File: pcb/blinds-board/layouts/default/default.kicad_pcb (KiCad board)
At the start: 2 copper layers, 87 parts

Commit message: feat(blinds-pcb): 6-layer placement + A* routing, board fully routed
tools/router.py is an A* grid router over the copper layers; place_and_render
holds the anchors, the passive banks and the fanout. 87 footprints, 62 routed
nets, 9241 segments, 238 vias, nothing left unrouted.

What it took, in the order the board taught it:
  * 6 layers (F/In1 GND/In2/In3/In4 GND/B). 24 nets escape a 4mm 29-pin QFN;
    two routing layers cannot do it and three got within a few nets.
  * Fanout stubs per fine-pitch pad, staggered over four depths, each ending
    in a via. Without the via the escapes stay 0.4mm apart forever and none of
    them can ever change layer — which is what stranded the last net.
  * L-shaped corner pads rasterised, not bounding-boxed: the box fills in the
    notch the neighbouring pin escapes through.
  * Clearance is width-aware at query time, so a 0.6mm rail cannot be laid at
    a 0.15mm track's clearance. That was a real short, found by DRC.
  * Local decoupling for PMID, BATP and REGN — a sense pin on the far flank of
    a QFN wants copper 3mm away, not 8.
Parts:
- J1: footprint USB_C_16P:USB-C_SMD-TYPE-C-31-M-12_1 -> XH_3AW:CONN-TH_3P-P2.50_XH-3A
- J4: footprint XH_3AW:CONN-TH_3P-P2.50_XH-3A -> XH_2AW:CONN-TH_2P-P2.50_XH-2AW
- J5: footprint XH_2AW:CONN-TH_2P-P2.50_XH-2AW -> USB_C_16P:USB-C_SMD-TYPE-C-31-M-12_1
- U2: footprint ESP32_C3_MINI_1:WIFIM-SMD_ESP32-C3-MINI-1 -> TLV62569DBVR:SOT-23-5_L3.0-W1.7-P0.95-LS2.8-BR
- U3: footprint TLV62569DBVR:SOT-23-5_L3.0-W1.7-P0.95-LS2.8-BR -> BQ25798RQMR:QFN-29_L4.0-W4.0-P0.40-TL-BQ25792RQMR
- U4: footprint BQ25798RQMR:QFN-29_L4.0-W4.0-P0.40-TL-BQ25792RQMR -> DRV8871DDAR:SO-8_L4.9-W3.9-P1.27-LS6.0-BL-EP
- U5: footprint DRV8871DDAR:SO-8_L4.9-W3.9-P1.27-LS6.0-BL-EP -> DRV5032FBDBZR:SOT-23_L2.9-W1.3-P1.90-LS2.4-BR
- U6: footprint DRV5032FBDBZR:SOT-23_L2.9-W1.3-P1.90-LS2.4-BR -> ESP32_C3_MINI_1:WIFIM-SMD_ESP32-C3-MINI-1
- moved U6 809.6 mm to (10.5, 12.0)
- moved C20 809.5 mm to (24.0, 75.5)
- moved J3 808.6 mm to (4.00, 64.8)
- moved J4 768.7 mm to (34.0, 64.8), turned to 180 degrees
- moved C22 763.3 mm to (7.00, 21.2)
- moved SW1 758.1 mm to (32.0, 14.3)
- moved C23 749.9 mm to (10.4, 21.2)
- moved SW2 748.0 mm to (32.0, 7.60)
- moved C21 747.9 mm to (2.40, 21.2)
- moved R20 719.7 mm to (20.6, 21.2)
- moved C18 713.1 mm to (17.2, 21.2)
- moved R9 706.5 mm to (13.8, 21.2)
- moved C11 685.7 mm to (16.5, 55.0)
- moved C13 683.3 mm to (29.0, 56.4)
- moved C12 663.2 mm to (29.0, 54.0)
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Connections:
- C20 pad 1: 1-3 -> 1-5
- C20 pad 2: 2 -> gnd_tab
- C28 pad 1: 1-5 -> 1-6
- J1 pad 1: 2 -> 1
- J1 pad 2: 2 -> batmid
- J2 pad 1: 1 -> 1-5
- J2 pad 2: batmid -> gnd_tab
- J2 pad 3: 2 -> hall_do_tab
- J4 pad 1: 1-3 -> mot_a
- J4 pad 2: 2 -> mot_b
- J5 pad 1: mot_a -> 2
- J5 pad 2: mot_b -> 2
- R16 pad 1: 1-6 -> 1-7
- R23 pad 1: 1-5 -> 1-6
- R27 pad 1: 1-5 -> 1-6
- U2 pad 1: 2 -> en_buck
- U2 pad 3: 1-3 -> sw_buck
- U2 pad 4: (no net) -> 1-2
- U2 pad 5: io2 -> fb_buck
- U3 pad 1: en_buck -> chg_stat
- U3 pad 2: 2 -> VBUS
- U3 pad 3: sw_buck -> VBUS
- U3 pad 4: 1-2 -> btst1
- U3 pad 5: fb_buck -> 1-6
- U4 pad 1: chg_stat -> 2
- U4 pad 2: VBUS -> 19
- U4 pad 3: VBUS -> 18
- U4 pad 4: btst1 -> ilim_mot
- U4 pad 5: 1-5 -> 1-1
- U4 pad 6: DP -> mot_a
- U4 pad 7: DM -> 2
- U4 pad 8: VBUS -> mot_b
- U4 pad 9: VBUS -> 2
- U5 pad 1: 2 -> 1-5
- U5 pad 2: 19 -> hall_do_tab
- U5 pad 3: 18 -> gnd_tab
- U6 pad 1: 1-3 -> 2
- U6 pad 2: hall_do -> 2
- U6 pad 3: 2 -> 1-3
- U7 pad 7: 1-6 -> 1-7
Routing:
- net 1-3: track 0.00 -> 110.0 mm, vias 0 -> 17
- net 18: track 0.00 -> 86.5 mm, vias 0 -> 3
- net 1-2: track 0.00 -> 83.3 mm, vias 0 -> 8
- net 2: track 0.00 -> 79.1 mm, vias 0 -> 54
- net 19: track 0.00 -> 75.6 mm, vias 0 -> 4
- net usb_dp: track 0.00 -> 70.6 mm, vias 0 -> 2
- net VBUS: track 0.00 -> 68.8 mm, vias 0 -> 12
- net 1: track 0.00 -> 59.0 mm, vias 0 -> 8
- net usb_dn: track 0.00 -> 58.4 mm, vias 0 -> 4
- net 2-2: track 0.00 -> 57.5 mm, vias 0 -> 3
- net hall_do: track 0.00 -> 57.2 mm, vias 0 -> 3
- net 1-1: track 0.00 -> 56.8 mm, vias 0 -> 9
- net en_bst: track 0.00 -> 41.4 mm, vias 0 -> 5
- net btn_up: track 0.00 -> 40.0 mm, vias 0 -> 2
- net sw_chg1: track 0.00 -> 39.6 mm, vias 0 -> 4
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- added copper zone on B.Cu, net gnd
- added copper zone on F.Cu, net gnd
- added copper zone on In1.Cu, net gnd
- added copper zone on In4.Cu, net gnd
- added copper zone on B.Cu, net gnd_tab
- added copper zone on F.Cu, net gnd_tab
- added copper zone on In1.Cu, net gnd_tab
- added copper zone on In4.Cu, net gnd_tab
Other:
- board outline added: 38 x 81 mm
- copper layers 2 -> 6
- rule pad_to_mask_clearance: 0 -> 0.05
- board text added: "0x63616c"
- board text added: "BAT 2S + M -"
- board text added: "BLINDS DRIVER rev B"
- board text added: "DOWN"
- board text added: "HALL"
- board text added: "HALL TAB - snap off"
- board text added: "MOTOR"
- board text added: "UP"
- board text added: "USB-C PD"

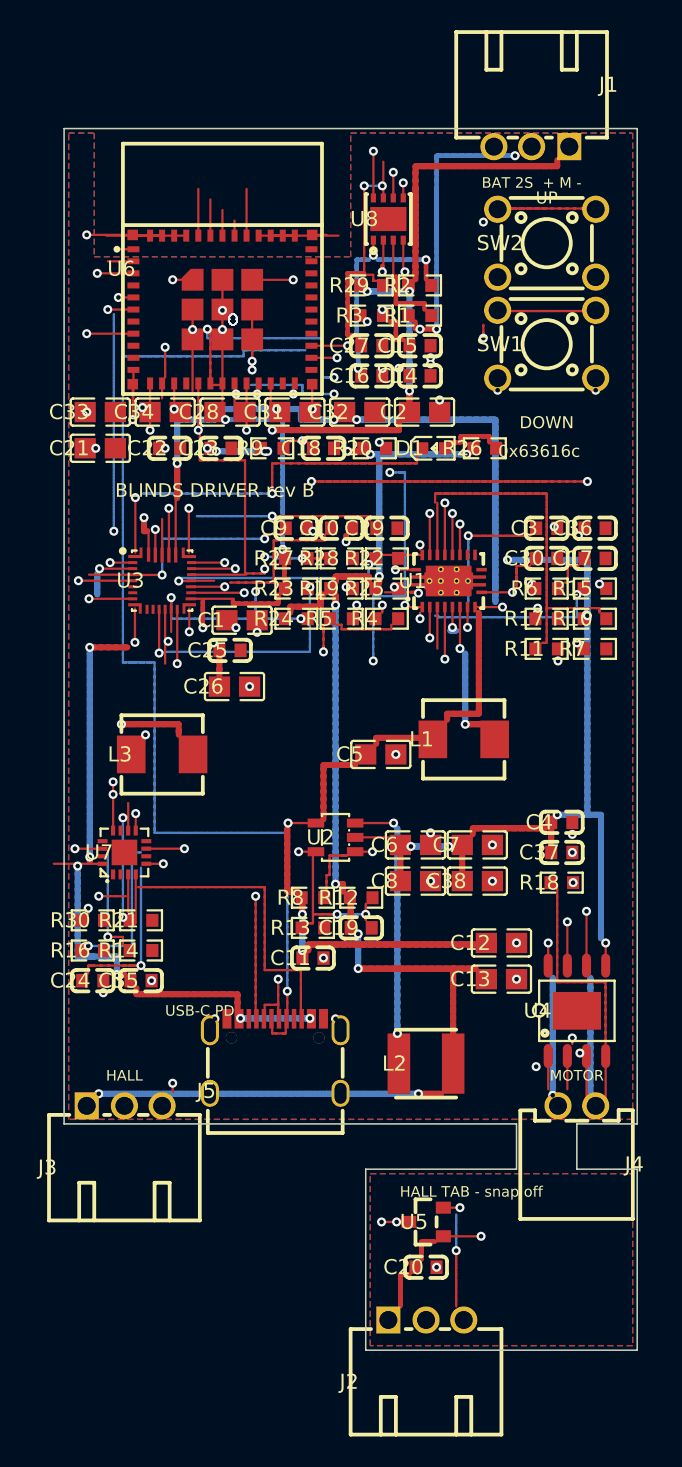
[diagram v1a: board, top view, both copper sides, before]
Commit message: feat(blinds-pcb): fab outputs, courtyards, silk trim, DRC harness
Adds the pieces the fab package needs and the checks that judge it:
  * courtyards on all 43 vendored footprints (add_courtyards.py) — KiCad ships
    missing_courtyard as an IGNORED check, so a board with none passes DRC
    while the overlap check silently never runs
  * silk trimmed back out of pads, once, per trim_lib_silk's warning
  * fix_vendor_pads.py: the TPS61088's eight netless 0.2mm thermal vias become
    PGND at 0.55/0.3, the USB-C's two mounting posts become non-plated
  * build_outputs.sh writes a net_settings block — DRC checks the NETCLASS
    clearance, and KiCad's built-in default of 0.2mm flagged every trace on a
    board designed to 0.13
  * gerbers (6 layers), drill, BOM, CPL and renders in fab/ and render/

DRC is NOT clean yet: 184 violations and 65 unconnected pads remain, mostly
marginal overlaps around through-hole pads and ground pads the pour does not
reach. Routing is 2 connections short. See issue #22 for the specifics.
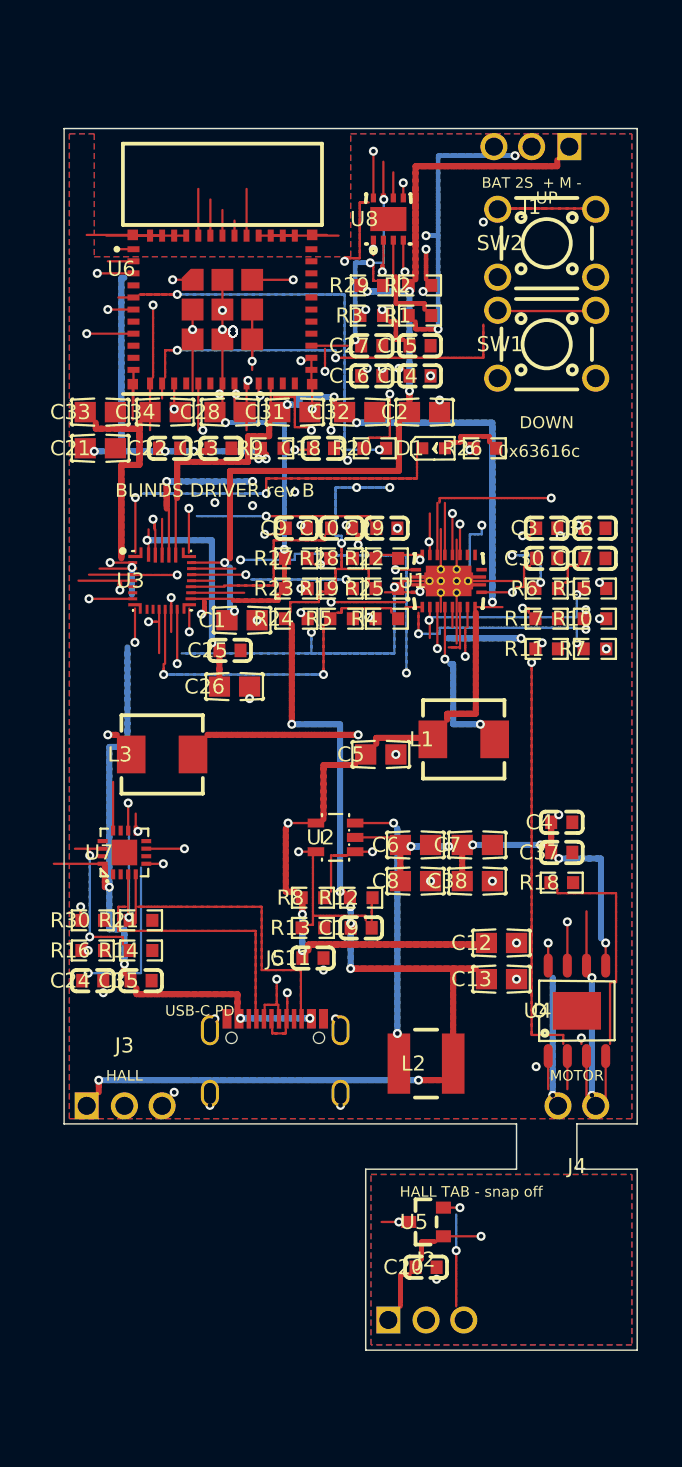
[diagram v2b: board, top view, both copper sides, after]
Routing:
- net 1-3: track 110.0 -> 129.3 mm, vias 17 -> 18
- net 2: track 79.1 -> 97.7 mm, vias 54 -> 45
- net 2-2: track 57.5 -> 42.9 mm, vias 3 -> 5
- net prog: track 15.8 -> 1.50 mm, vias 2 -> 0
- net 18: track 86.5 -> 73.1 mm, vias 3 -> 5
- net usb_dp: track 70.6 -> 57.4 mm, vias 2 -> 3
- net 1-6: track 33.1 -> 40.5 mm
- net batmid: track 22.8 -> 29.9 mm
- net sw_chg1: track 39.6 -> 32.8 mm
- net sda: track 36.6 -> 43.3 mm, vias 3 -> 4
- net 19: track 75.6 -> 69.4 mm, vias 4 -> 2
- net boot_bst: track 9.85 -> 15.5 mm
- net 1-1: track 56.8 -> 61.9 mm, vias 9 -> 11
- net chg_int: track 27.1 -> 22.8 mm
- net CC1: track 22.2 -> 18.9 mm, vias 2 -> 0
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- added copper zone on B.Cu, net 2
- added copper zone on F.Cu, net 2
- added copper zone on In1.Cu, net 2
- added copper zone on In4.Cu, net 2
- removed copper zone on B.Cu, net gnd
- removed copper zone on F.Cu, net gnd
- removed copper zone on In1.Cu, net gnd
- removed copper zone on In4.Cu, net gnd

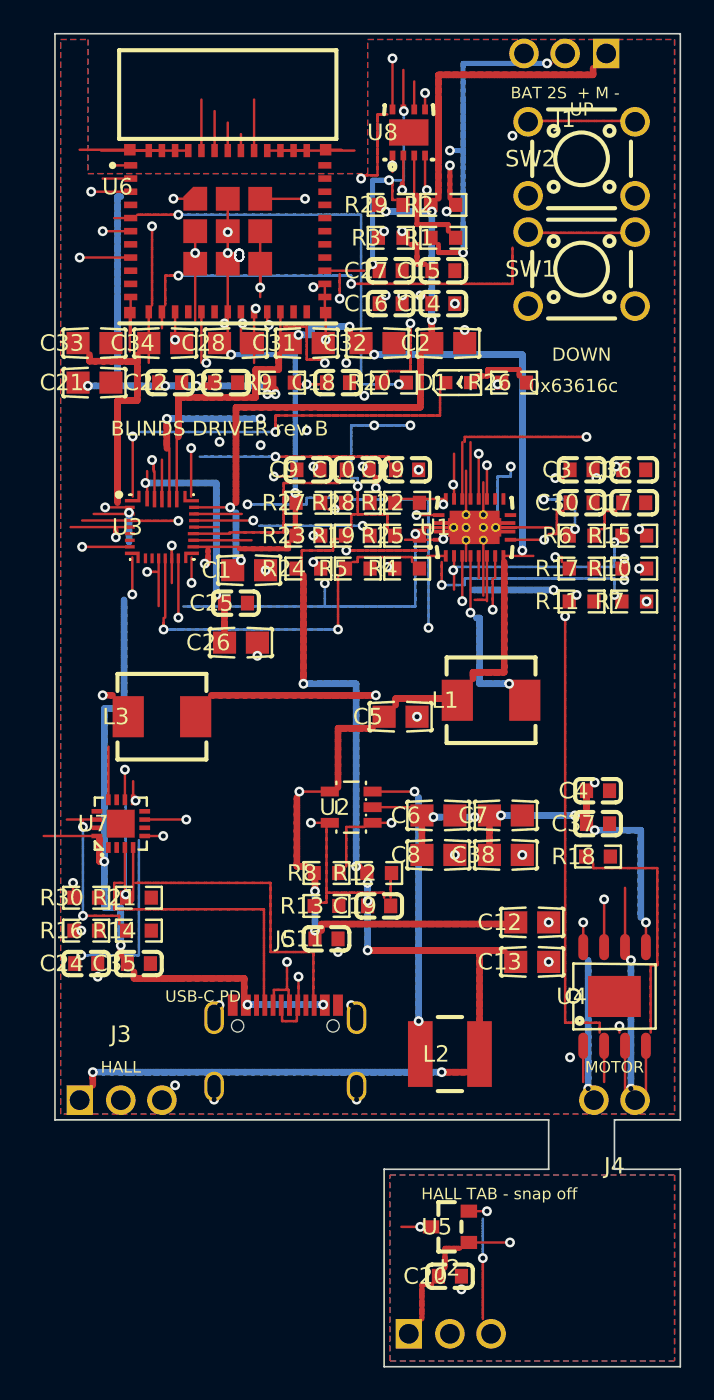
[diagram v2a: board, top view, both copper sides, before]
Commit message: fix(blinds-pcb): five router bugs that DRC was reporting as 350 violations
Down to 37 from 350. Each one was a modelling error, not a hundred separate
layout problems:

  * pad.layers was read with str(), which on a pyzig list gives its object
    repr — so EVERY pad fell back to F.Cu alone and the router ran tracks
    through every through-hole pad on the inner and bottom layers
  * trim_lib_silk leaves a zero-length layerless fp_line behind for each silk
    segment it clips away; a layerless line inherits the footprint's layer,
    which is F.Cu, so 28 of them were netless copper on the connectors
  * pad_shape was keyed by pad NAME, and the TPS61088 has nine pads called 21
    (the land plus eight thermal vias) — only the last one got a clearance halo
  * routes could start or end on halo cells, which carry the net id but are not
    copper, so some tracks were emitted floating
  * netless pads were blocked with clearance but no allowance for track width

Fab package (6-layer gerbers, drill, BOM, CPL) regenerated in fab/.
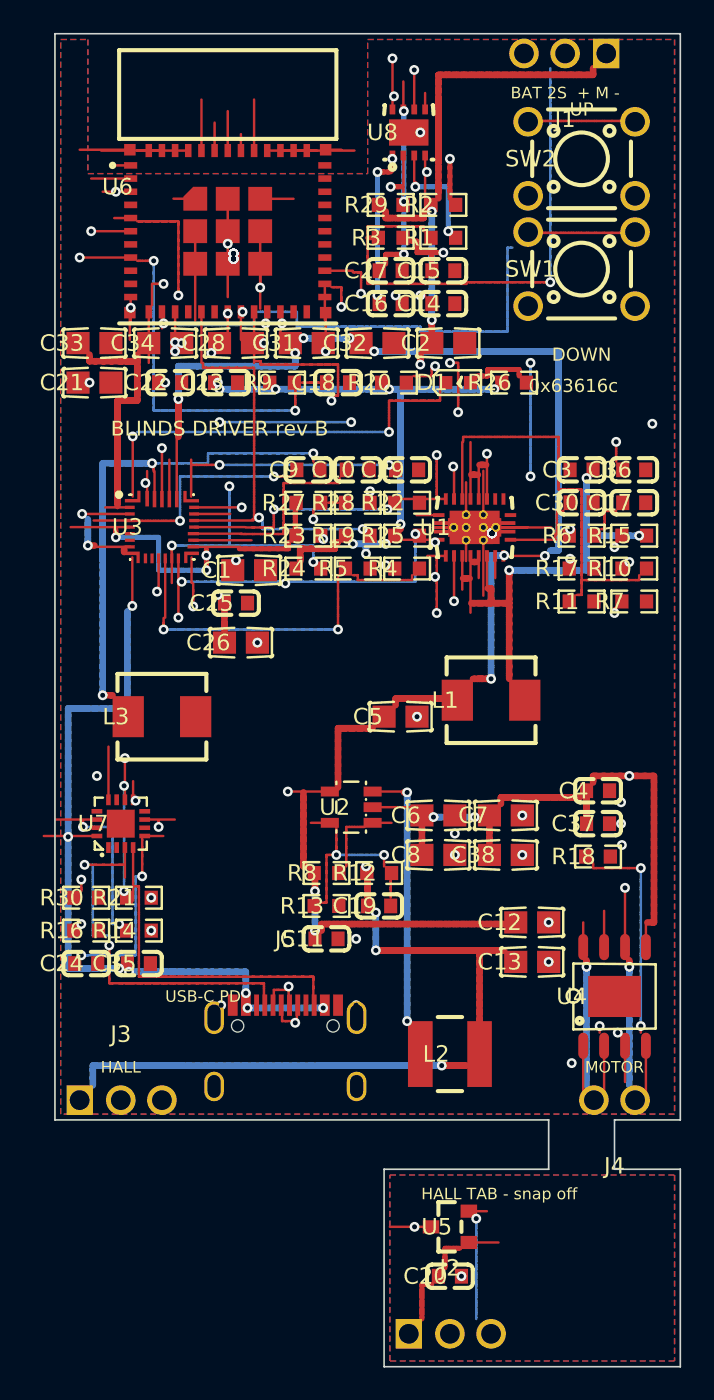
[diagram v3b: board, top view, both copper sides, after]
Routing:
- net 2-2: track 42.9 -> 2.40 mm, vias 5 -> 0
- net usb_dp: track 57.4 -> 77.2 mm, vias 3 -> 4
- net 1-3: track 129.3 -> 111.2 mm, vias 18 -> 16
- net boot_bst: track 15.5 -> 1.35 mm, vias 2 -> 0
- net ov_out: track 33.8 -> 45.8 mm
- net prog: track 1.50 -> 12.8 mm, vias 0 -> 2
- net usb_dn: track 55.2 -> 64.4 mm, vias 3 -> 4
- net 1-6: track 40.5 -> 33.0 mm
- net 2-3: track 10.6 -> 17.3 mm
- net ilim_bst: track 14.1 -> 20.4 mm
- net vcc_bst: track 16.9 -> 22.2 mm, vias 3 -> 2
- net btn_up: track 40.1 -> 44.9 mm, vias 2 -> 1
- net 18: track 73.1 -> 77.9 mm
- net VBUS: track 65.6 -> 70.3 mm, vias 8 -> 9
- net 1-2: track 80.8 -> 85.5 mm, vias 7 -> 11
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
